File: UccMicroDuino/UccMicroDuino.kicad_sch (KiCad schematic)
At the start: 8 parts, among them J2 Conn_01x10_Socket, J2 USB_A, U2 ATtiny85-20S

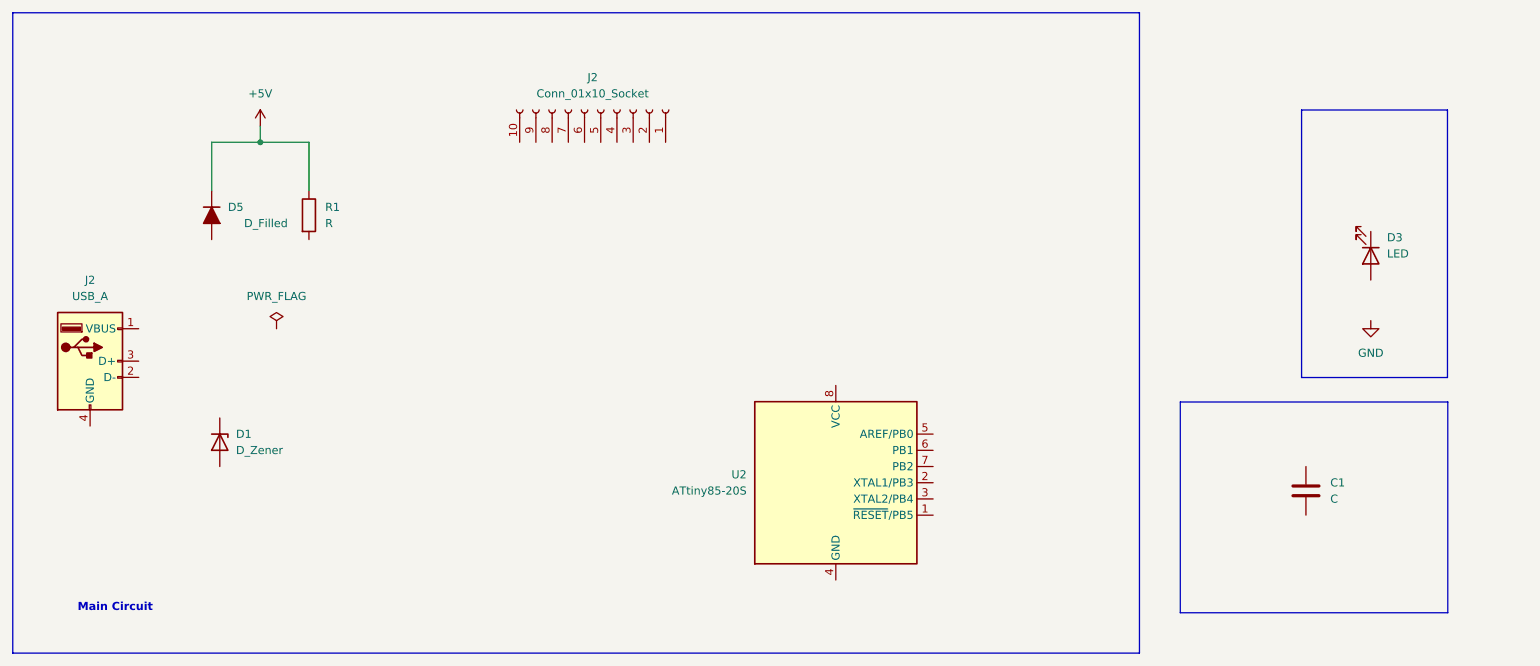
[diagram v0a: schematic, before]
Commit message: modificamos plano terminado el circuito
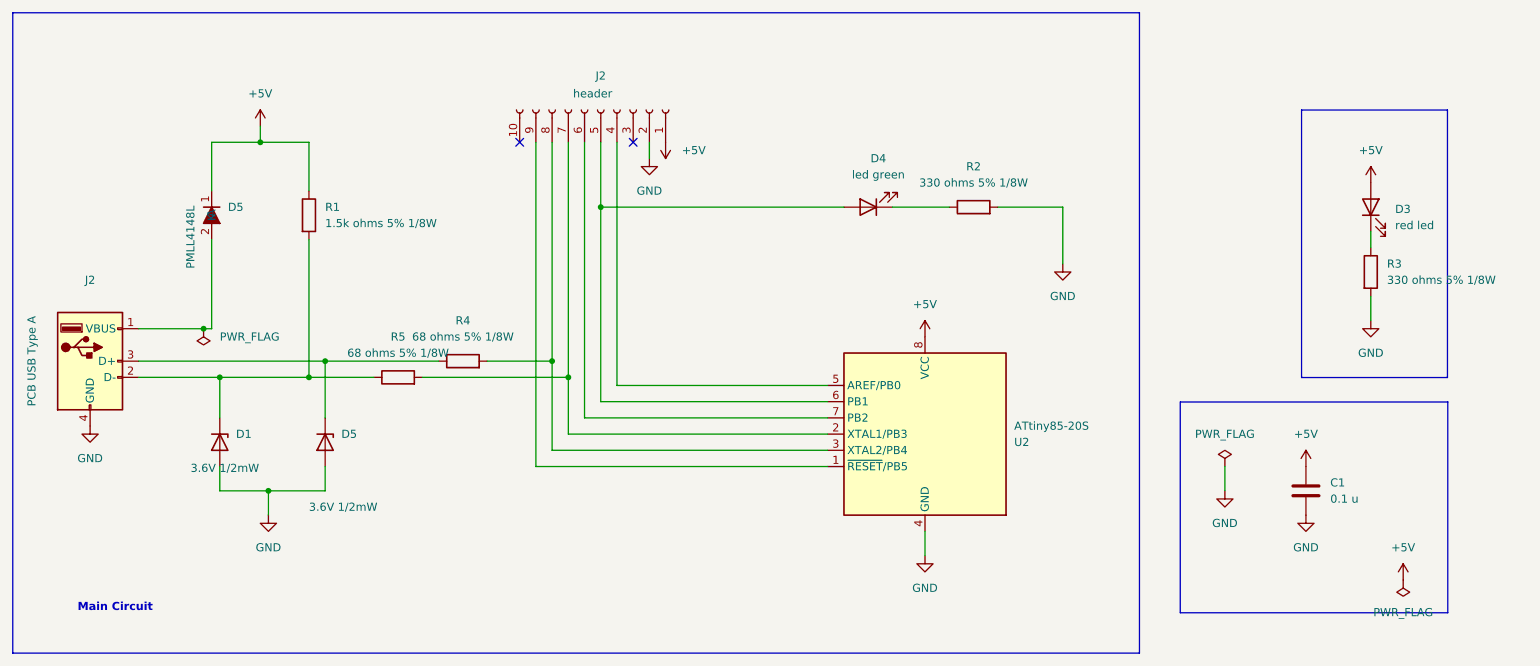
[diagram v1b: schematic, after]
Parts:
- added D4: led green, symbol Device:LED
- added D5: 3.6V 1/2mW, Diode_SMD:D_SOD-123, symbol Device:D_Zener
- added R2, R3: 330 ohms 5% 1/8W, symbol Device:R
- added R4, R5: 68 ohms 5% 1/8W, Resistor_SMD:R_0805_2012Metric_Pad1.20x1.40mm_HandSolder, symbol Device:R
- C1: value C -> 0.1 u
- D1: value D_Zener -> 3.6V 1/2mW
- D3: value LED -> red led
- D5: value D_Filled -> PMLL4148L
- J2: value Conn_01x10_Socket -> header
- J2: value USB_A -> PCB USB Type A
- R1: value R -> 1.5k ohms 5% 1/8W
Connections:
- net +5V: now also C1.1, D3.2 (A), J2.1 (Pin_1), U2.8 (VCC)
- net GND: now also C1.2, D1.2 (A), J2.2 (Pin_2), J2.4 (GND), U2.4 (GND), D5.2 (A), R2.2, R3.2
- net at D3.1 (K): now also R3.1
- net at R1.2: now also D1.1 (K), J2.2 (D-), R5.1
- net at U2.1 (~{RESET}/PB5): now also J2.9 (Pin_9)
- net at U2.2 (XTAL1/PB3): now also J2.7 (Pin_7), R5.2
- net at U2.3 (XTAL2/PB4): now also J2.8 (Pin_8), R4.2
- net at U2.5 (AREF/PB0): now also J2.4 (Pin_4)
- net at U2.6 (PB1): now also J2.5 (Pin_5), D4.2 (A)
- net at U2.7 (PB2): now also J2.6 (Pin_6)
- net at J2.1 (VBUS): now also D5.2 (A)
- net at J2.3 (D+): now also D5.1 (K), R4.1
- new net: D4.1 (K), R2.1
- no-connect marks 0 -> 2
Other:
- moved on the sheet: D3, U2
